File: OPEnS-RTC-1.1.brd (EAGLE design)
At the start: 22.9 x 83.6 mm, 58 parts, among them U1 FRAM, U2 DS3231ST&R

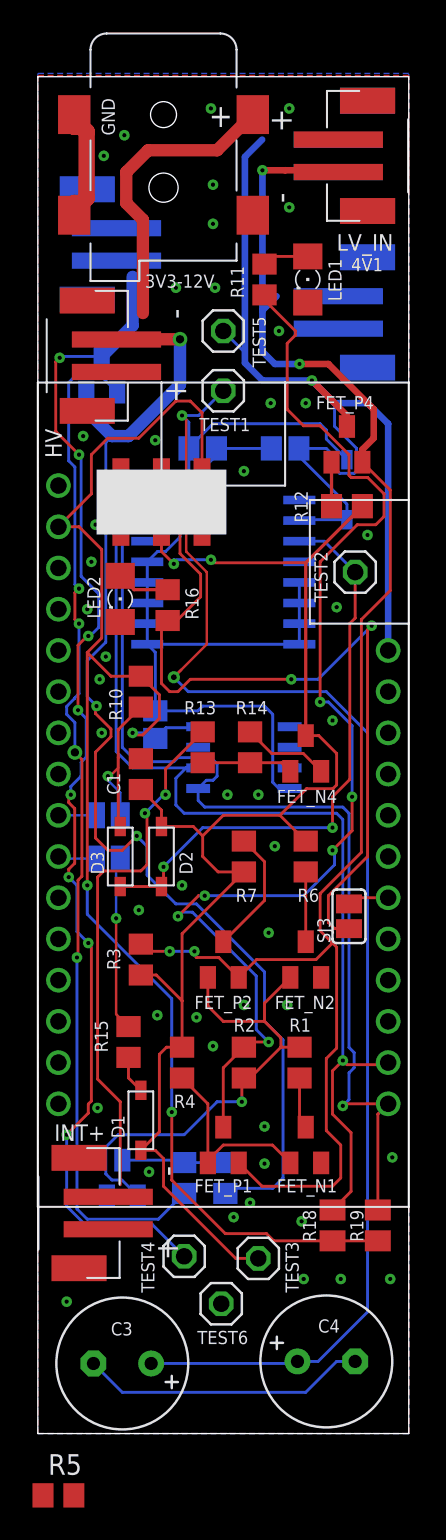
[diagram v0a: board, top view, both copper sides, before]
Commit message: Revised components and labels.
Added documentation (with BoM) as a .docx and .pdf. Swapped pins on JST connectors. Removed pointless pullup resistor, added current limiting resistor for LED. Swapped 2mm barrel jack for 0.9mm x 3.2mm barrel jack. Combined components into OPEnS-RTC.lbr.
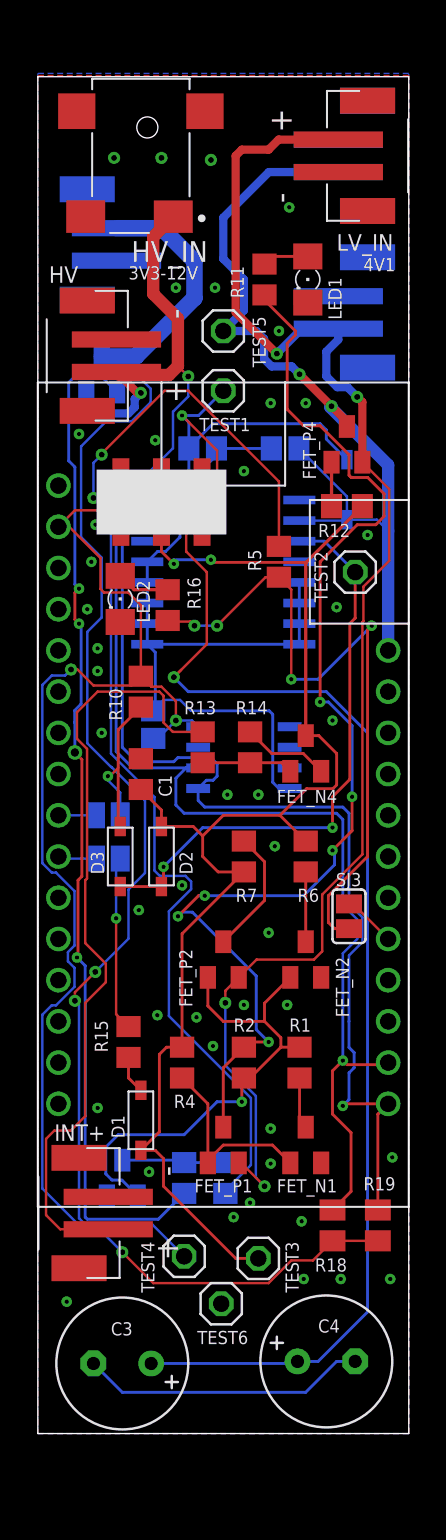
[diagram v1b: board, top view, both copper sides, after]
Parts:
- removed R3: 10k, rcl:R0805
- FEATHER: device bluefruit_m0:BLUEFRUIT_MO -> OPEnS-RTC:BLUEFRUIT_MO
- HV_IN: value (none) -> PJ-028-SMT-TR; device adafruit:DCJACK_2MM_SMT -> OPEnS-RTC:CUI_PJ-028-SMT-TR
- moved R5 59.1 mm to (14.9, 49.9), turned to 270 degrees
- moved HV_IN 2.90 mm to (6.35, 74.9), turned to 180 degrees
- moved C2 0.13 mm to (7.11, 39.9)
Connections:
- removed net N$20: FEATHER.10, SJ3.2
- new net N$17: FEATHER.9, SJ3.2
- net +4.1V: no longer R3.2
- net GND: now also HV_IN.2, HV_IN.3, HV_IN.3.1; no longer HV_IN.GND, HV_IN.GNDBREAK
- net VCC_HV: now also HV_IN.1; no longer HV_IN.PWR1
- net V_LATCH: no longer R3.1
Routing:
- net N$16: track 0.00 -> 26.6 mm, vias 0 -> 2
- net INT+: track 32.7 -> 48.4 mm, vias 2 -> 0
- net VCC_HV: track 93.1 -> 80.7 mm, vias 3 -> 2
- net LOAD_HV: track 73.2 -> 83.0 mm, vias 8 -> 2
- net +4.1V: track 97.3 -> 89.0 mm
- net LOAD_LV: track 62.8 -> 55.2 mm, vias 1 -> 2
- net OVR_READ: track 49.4 -> 42.0 mm, vias 2 -> 4
- net GND: track 78.4 -> 71.3 mm, vias 46 -> 43
- net +3V3: track 89.9 -> 94.8 mm
- net N$17: track 0.00 -> 3.31 mm
- net V_LATCH: track 89.4 -> 86.2 mm
- net N$20: track 2.57 -> 0.00 mm
- net V_BACKUP: track 105.6 -> 107.4 mm
- net SCL: track 64.6 -> 65.3 mm
- net SDA: track 62.3 -> 63.0 mm
